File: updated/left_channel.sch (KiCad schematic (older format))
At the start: 20 parts, among them J2 Left 8 ohms, J3 Left 0 ohms, J7 Conn_Coaxial, T1 AudioTxfmr

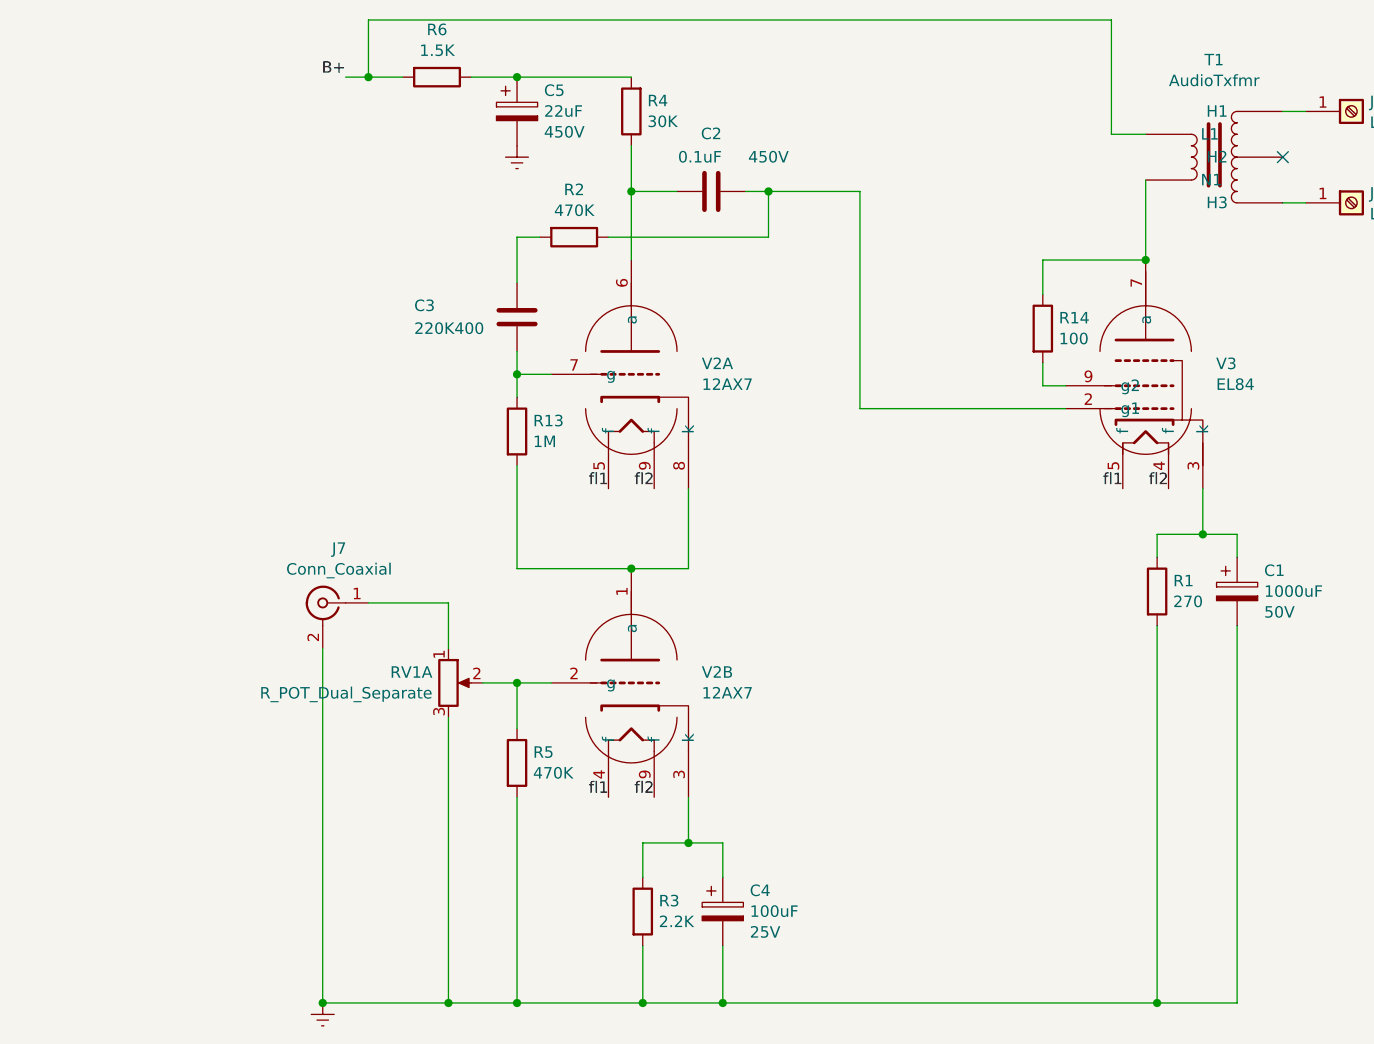
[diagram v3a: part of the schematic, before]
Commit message: adding some components to try to stop a high pitch squal sound I sometimes hear from the amp
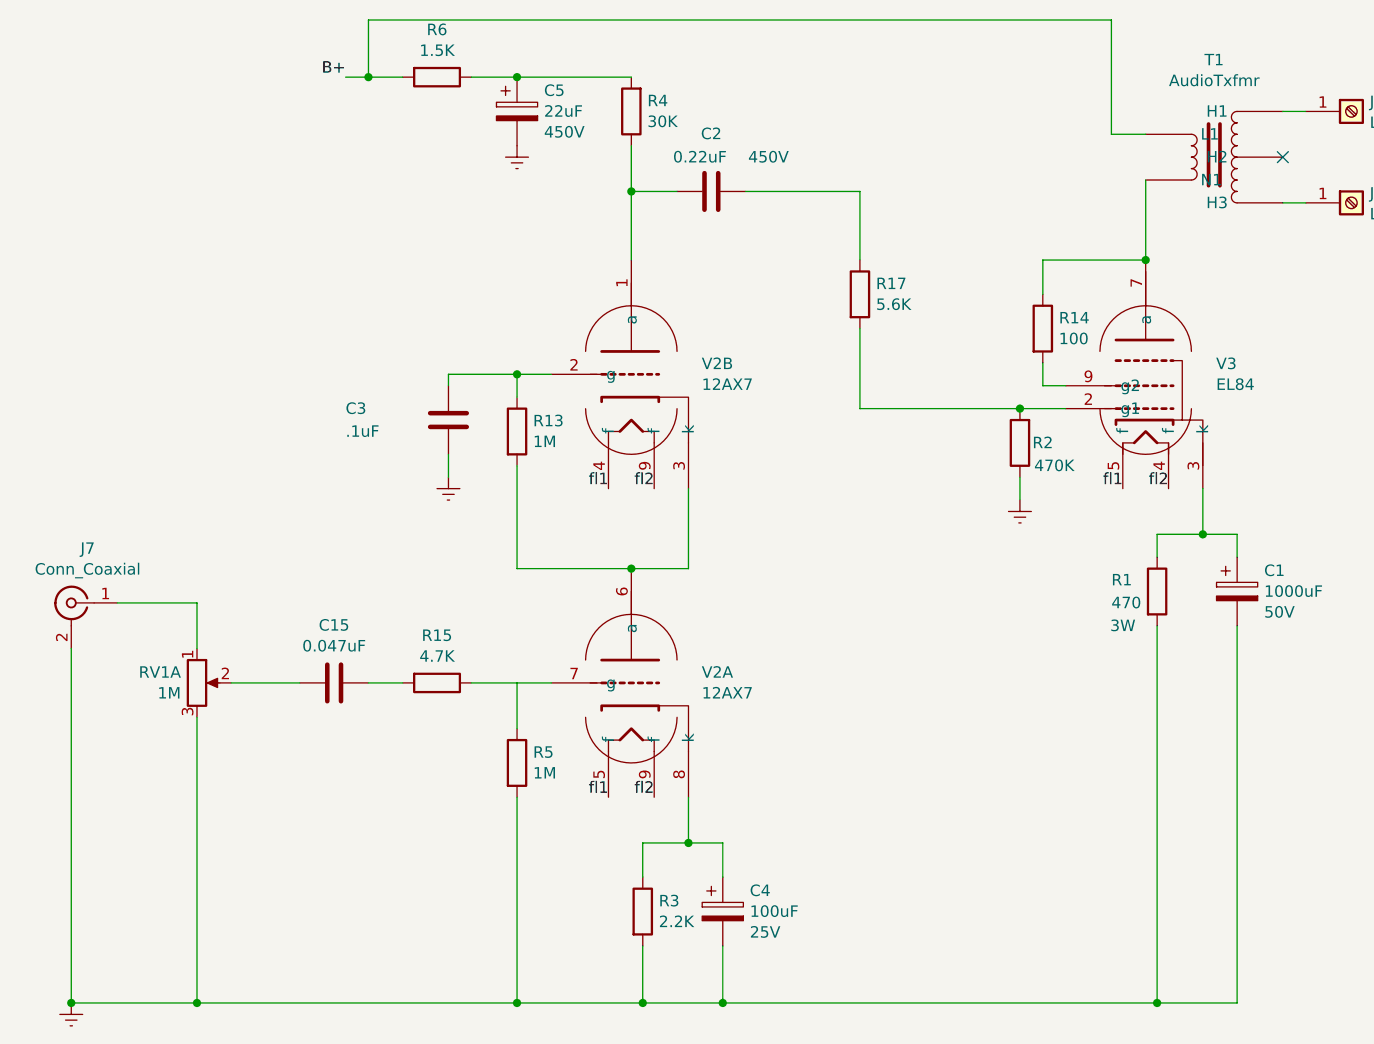
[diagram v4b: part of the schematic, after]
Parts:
- added C15: 0.047uF, symbol Device:C
- added R15: 4.7K, symbol Device:R
- added R17: 5.6K, symbol Device:R
- C2: value 0.1uF -> 0.22uF
- C3: value 220K400 -> .1uF
- R1: value 270 -> 470; Power 5W -> 3W
- R5: value 470K -> 1M
- RV1: value R_POT_Dual_Separate -> 1M
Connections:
- net Earth: now also C3.2, R2.1
- net at C2.2, R4.1: now also V2.1 (a); no longer V2.6 (a)
- net at C4.1, R3.1: now also V2.8 (k); no longer V2.3 (k)
- net at R2.2: now also V3.2 (g1), R17.2; no longer C3.1
- new net: R13.2, V2.3 (k), V2.6 (a)
- new net: R15.1, R5.1, V2.7 (g)
- new net: C3.1, R13.1, V2.2 (g)
- new net: C2.1, R17.1
- new net: C15.2, RV1.2
- new net: C15.1, R15.2
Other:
- moved on the sheet: C3, J7, R2, RV1A, V2A, V2B
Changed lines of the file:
@@
 $Descr A4 11693 8268
 encoding utf-8
-Sheet 3 5
+Sheet 3 4
 Title ""
 Date ""
@@
 AR Path="/5F1F04D2/5F1FED5C" Ref="C2"  Part="1"
 F 0 "C2" V 4898 2350 50  0000 C CNN
-F 1 "0.1uF" V 5000 2300 50  0000 C CNN
+F 1 "0.22uF" V 5000 2300 50  0000 C CNN
 F 2 "Capacitor_THT:CP_Radial_D4.0mm_P2.00mm" H 5188 2200 50  0001 C CNN
 F 3 "~" H 5150 2350 50  0001 C CNN
@@
 L Device:R R?
 U 1 1 5F1FED63
-P 4550 2550
+P 6500 3450
 AR Path="/5F1FED63" Ref="R?"  Part="1"
 AR Path="/5F1F04D2/5F1FED63" Ref="R2"  Part="1"
-F 0 "R2" V 4343 2550 50  0000 C CNN
-F 1 "470K" V 4434 2550 50  0000 C CNN
-F 2 "Resistor_THT:R_Axial_DIN0516_L15.5mm_D5.0mm_P20.32mm_Horizontal" V 4480 2550 50  0001 C CNN
-F 3 "~" H 4550 2550 50  0001 C CNN
-	1    4550 2550
-	0    1    1    0
+F 0 "R2" H 6400 3450 50  0000 C CNN
+F 1 "470K" H 6350 3550 50  0000 C CNN
+F 2 "Resistor_THT:R_Axial_DIN0516_L15.5mm_D5.0mm_P20.32mm_Horizontal" V 6430 3450 50  0001 C CNN
+F 3 "~" H 6500 3450 50  0001 C CNN
+	1    6500 3450
+	-1   0    0    1
 $EndComp
 $Comp
 L Device:C C?
 U 1 1 5F1FED69
-P 4300 2900
+P 4000 3350
 AR Path="/5F1FED69" Ref="C?"  Part="1"
 AR Path="/5F1F04D2/5F1FED69" Ref="C3"  Part="1"
-F 0 "C3" H 3850 2950 50  0000 L CNN
-F 1 "220K400" H 3850 2850 50  0000 L CNN
-F 2 "Capacitor_THT:CP_Radial_D10.0mm_P2.50mm" H 4338 2750 50  0001 C CNN
-F 3 "~" H 4300 2900 50  0001 C CNN
-	1    4300 2900
+F 0 "C3" H 3550 3400 50  0000 L CNN
+F 1 ".1uF" H 3550 3300 50  0000 L CNN
+F 2 "Capacitor_THT:CP_Radial_D10.0mm_P2.50mm" H 4038 3200 50  0001 C CNN
+F 3 "~" H 4000 3350 50  0001 C CNN
+	1    4000 3350
 	1    0    0    -1
 $EndComp
@@
 L Connector:Conn_Coaxial J?
 U 1 1 5F1FED7F
-P 3450 4150
+P 2350 4150
 AR Path="/5F1FED7F" Ref="J?"  Part="1"
 AR Path="/5F1F04D2/5F1FED7F" Ref="J7"  Part="1"
-F 0 "J7" H 3378 4388 50  0000 C CNN
-F 1 "Conn_Coaxial" H 3378 4297 50  0000 C CNN
-F 2 "" H 3450 4150 50  0001 C CNN
-F 3 " ~" H 3450 4150 50  0001 C CNN
-	1    3450 4150
+F 0 "J7" H 2278 4388 50  0000 C CNN
+F 1 "Conn_Coaxial" H 2278 4297 50  0000 C CNN
+F 2 "" H 2350 4150 50  0001 C CNN
+F 3 " ~" H 2350 4150 50  0001 C CNN
+	1    2350 4150
 	-1   0    0    -1
 $EndComp
 Wire Wire Line
-	4000 4650 4000 5900
-Wire Wire Line
-	4000 5900 3450 5900
-Wire Wire Line
-	3450 5900 3450 4350
+	2900 4650 2900 5900
+Wire Wire Line
+	2900 5900 2350 5900
+Wire Wire Line
+	2350 5900 2350 4350
 $Comp
 L power:Earth #PWR?
 U 1 1 5F1FED8E
-P 3450 5900
+P 2350 5900
 AR Path="/5F1FED8E" Ref="#PWR?"  Part="1"
 AR Path="/5F1F04D2/5F1FED8E" Ref="#PWR06"  Part="1"
-F 0 "#PWR06" H 3450 5650 50  0001 C CNN
-F 1 "Earth" H 3450 5750 50  0001 C CNN
-F 2 "" H 3450 5900 50  0001 C CNN
-F 3 "~" H 3450 5900 50  0001 C CNN
-	1    3450 5900
-	1    0    0    -1
-$EndComp
-Connection ~ 3450 5900
-Wire Wire Line
-	3650 4150 4000 4150
-Wire Wire Line
-	4000 4150 4000 4350
-Wire Wire Line
-	4150 4500 4300 4500
+F 0 "#PWR06" H 2350 5650 50  0001 C CNN
+F 1 "Earth" H 2350 5750 50  0001 C CNN
+F 2 "" H 2350 5900 50  0001 C CNN
+F 3 "~" H 2350 5900 50  0001 C CNN
+	1    2350 5900
+	1    0    0    -1
+$EndComp
+Connection ~ 2350 5900
+Wire Wire Line
+	2550 4150 2900 4150
+Wire Wire Line
+	2900 4150 2900 4350
 Text Label 4700 3650 2    50   ~ 0
 fl1
@@
 AR Path="/5F1F04D2/5F1FED9C" Ref="R5"  Part="1"
 F 0 "R5" H 4370 4896 50  0000 L CNN
-F 1 "470K" H 4370 4805 50  0000 L CNN
+F 1 "1M" H 4370 4805 50  0000 L CNN
 F 2 "Resistor_THT:R_Axial_DIN0516_L15.5mm_D5.0mm_P20.32mm_Horizontal" V 4230 4850 50  0001 C CNN
 F 3 "~" H 4300 4850 50  0001 C CNN
@@
 Wire Wire Line
 	4300 4700 4300 4500
-Connection ~ 4300 4500
 Wire Wire Line
 	4300 4500 4450 4500
@@
 $EndComp
 Wire Wire Line
-	4300 5900 4000 5900
+	4300 5900 2900 5900
 Wire Wire Line
 	4300 5000 4300 5900
-Connection ~ 4000 5900
-Connection ~ 4300 5900
+Connection ~ 2900 5900
 Wire Wire Line
 	5200 5650 5200 5900
@@
 	4850 5900 5200 5900
 Wire Wire Line
-	4300 3050 4300 3150
-Wire Wire Line
 	4450 3150 4300 3150
-Connection ~ 4300 3150
 Wire Wire Line
 	4300 3150 4300 3250
-Wire Wire Line
-	5300 2350 5400 2350
-Wire Wire Line
-	4400 2550 4300 2550
-Wire Wire Line
-	4300 2550 4300 2750
-Wire Wire Line
-	4700 2550 5400 2550
-Wire Wire Line
-	5400 2550 5400 2350
-Connection ~ 5400 2350
-Wire Wire Line
-	5400 2350 5800 2350
 NoConn ~ 7650 2200
 $Comp
@@
 	7750 2000 7650 2000
 Wire Wire Line
-	6700 3300 5800 3300
-Wire Wire Line
-	5800 3300 5800 2350
+	6700 3300 6500 3300
 Text Label 6950 3650 2    50   ~ 0
 fl1
@@
 AR Path="/5F1FEE00" Ref="R?"  Part="1"
 AR Path="/5F1F04D2/5F1FEE00" Ref="R1"  Part="1"
-F 0 "R1" H 7170 4146 50  0000 L CNN
-F 1 "270" H 7170 4055 50  0000 L CNN
+F 0 "R1" H 6900 4150 50  0000 L CNN
+F 1 "470" H 6900 4050 50  0000 L CNN
 F 2 "Resistor_THT:R_Axial_DIN0516_L15.5mm_D5.0mm_P20.32mm_Horizontal" V 7030 4100 50  0001 C CNN
 F 3 "~" H 7100 4100 50  0001 C CNN
-F 4 "5W" H 7100 4100 50  0001 C CNN "Power"
+F 4 "3W" H 6950 3950 50  0000 C CNN "Power"
 	1    7100 4100
 	1    0    0    -1
@@
 L local:12AX7 V2
 U 1 1 5F1EB7D2
+P 4800 4450
+F 0 "V2" H 5108 4446 50  0000 L CNN
+F 1 "12AX7" H 5108 4355 50  0000 L CNN
+F 2 "Valve:Valve_ECC-83-1" H 4820 4450 50  0001 C CNN
+F 3 "" H 4820 4450 50  0001 C CNN
+	1    4800 4450
+	1    0    0    -1
+$EndComp
+Wire Wire Line
+	4300 4000 4800 4000
+$Comp
+L local:12AX7 V2
+U 2 1 5F1F6427
 P 4800 3100
 F 0 "V2" H 5108 3096 50  0000 L CNN
@@
 F 2 "Valve:Valve_ECC-83-1" H 4820 3100 50  0001 C CNN
 F 3 "" H 4820 3100 50  0001 C CNN
-	1    4800 3100
-	1    0    0    -1
-$EndComp
-Wire Wire Line
-	4300 4000 4800 4000
-$Comp
-L local:12AX7 V2
-U 2 1 5F1F6427
-P 4800 4450
-F 0 "V2" H 5108 4446 50  0000 L CNN
-F 1 "12AX7" H 5108 4355 50  0000 L CNN
-F 2 "Valve:Valve_ECC-83-1" H 4820 4450 50  0001 C CNN
-F 3 "" H 4820 4450 50  0001 C CNN
-	2    4800 4450
+	2    4800 3100
 	1    0    0    -1
 $EndComp
@@
 L Device:R_POT_Dual_Separate RV1
 U 1 1 5F23DDB3
-P 4000 4500
-F 0 "RV1" H 3930 4546 50  0000 R CNN
-F 1 "R_POT_Dual_Separate" H 3930 4455 50  0000 R CNN
-F 2 "" H 4000 4500 50  0001 C CNN
-F 3 "~" H 4000 4500 50  0001 C CNN
-	1    4000 4500
-	1    0    0    -1
-$EndComp
+P 2900 4500
+F 0 "RV1" H 2830 4546 50  0000 R CNN
+F 1 "1M" H 2830 4455 50  0000 R CNN
+F 2 "" H 2900 4500 50  0001 C CNN
+F 3 "~" H 2900 4500 50  0001 C CNN
+	1    2900 4500
+	1    0    0    -1
+$EndComp
+$Comp
+L Device:C C?
+U 1 1 5F5B00D6
+P 3500 4500
+AR Path="/5F200EB9/5F5B00D6" Ref="C?"  Part="1"
+AR Path="/5F1F04D2/5F5B00D6" Ref="C15"  Part="1"
+F 0 "C15" V 3248 4500 50  0000 C CNN
+F 1 "0.047uF" V 3339 4500 50  0000 C CNN
+F 2 "" H 3538 4350 50  0001 C CNN
+F 3 "~" H 3500 4500 50  0001 C CNN
+	1    3500 4500
+	0    1    1    0
+$EndComp
+$Comp
+L Device:R R?
+U 1 1 5F5B00DC
+P 3950 4500
+AR Path="/5F200EB9/5F5B00DC" Ref="R?"  Part="1"
+AR Path="/5F1F04D2/5F5B00DC" Ref="R15"  Part="1"
+F 0 "R15" V 3743 4500 50  0000 C CNN
+F 1 "4.7K" V 3834 4500 50  0000 C CNN
+F 2 "" V 3880 4500 50  0001 C CNN
+F 3 "~" H 3950 4500 50  0001 C CNN
+	1    3950 4500
+	0    1    1    0
+$EndComp
+Wire Wire Line
+	3650 4500 3800 4500
+Wire Wire Line
+	4100 4500 4300 4500
+Wire Wire Line
+	3050 4500 3350 4500
+Connection ~ 4300 5900
+$Comp
+L power:Earth #PWR?
+U 1 1 5F5C6D43
+P 6500 3700
+AR Path="/5F200EB9/5F5C6D43" Ref="#PWR?"  Part="1"
+AR Path="/5F1F04D2/5F5C6D43" Ref="#PWR011"  Part="1"
+F 0 "#PWR011" H 6500 3450 50  0001 C CNN
+F 1 "Earth" H 6500 3550 50  0001 C CNN
+F 2 "" H 6500 3700 50  0001 C CNN
+F 3 "~" H 6500 3700 50  0001 C CNN
+	1    6500 3700
+	1    0    0    -1
+$EndComp
+Wire Wire Line
+	6500 3700 6500 3600
+Connection ~ 6500 3300
+Wire Wire Line
+	6500 3300 5800 3300
+Wire Wire Line
+	5300 2350 5800 2350
+$Comp
+L power:Earth #PWR?
+U 1 1 5F5E593F
+P 4000 3600
+AR Path="/5F200EB9/5F5E593F" Ref="#PWR?"  Part="1"
+AR Path="/5F1F04D2/5F5E593F" Ref="#PWR010"  Part="1"
+F 0 "#PWR010" H 4000 3350 50  0001 C CNN
+F 1 "Earth" H 4000 3450 50  0001 C CNN
+F 2 "" H 4000 3600 50  0001 C CNN
+F 3 "~" H 4000 3600 50  0001 C CNN
+	1    4000 3600
+	1    0    0    -1
+$EndComp
+Wire Wire Line
+	4000 3600 4000 3500
+Wire Wire Line
+	4300 3150 4000 3150
+Wire Wire Line
+	4000 3150 4000 3200
+Connection ~ 4300 3150
+$Comp
+L Device:R R?
+U 1 1 5F5F04AC
+P 5800 2800
+AR Path="/5F200EB9/5F5F04AC" Ref="R?"  Part="1"
+AR Path="/5F1F04D2/5F5F04AC" Ref="R17"  Part="1"
+F 0 "R17" H 5870 2846 50  0000 L CNN
+F 1 "5.6K" H 5870 2755 50  0000 L CNN
+F 2 "" V 5730 2800 50  0001 C CNN
+F 3 "~" H 5800 2800 50  0001 C CNN
+	1    5800 2800
+	1    0    0    -1
+$EndComp
+Wire Wire Line
+	5800 2650 5800 2350
+Wire Wire Line
+	5800 2950 5800 3300
 $EndSCHEMATC

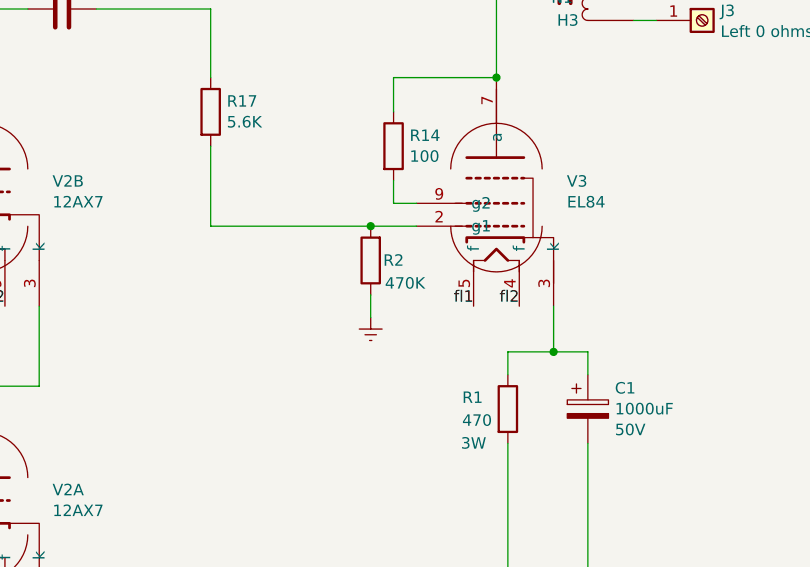
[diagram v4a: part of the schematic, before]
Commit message: change EL84 grid leak resistor to 1M
In the day time, I sort of feel the amp is too quiet. That adding the 5.6k resistor inline has reduced the signal. This small resistance divide is like 98% the input. But that is still the 2% loss of signal. I think the gain stage of these preamp tubes is not very strong. And I read the EL84 does have a wider response to small changes in input impedance.
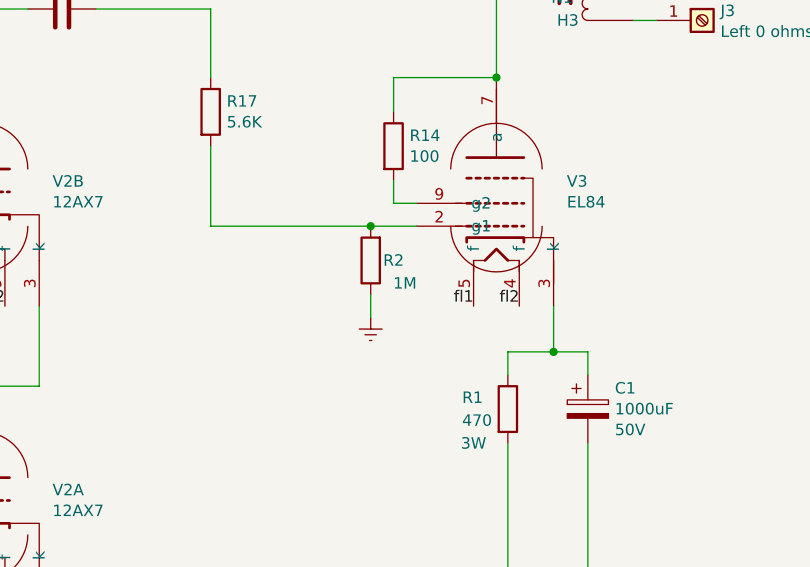
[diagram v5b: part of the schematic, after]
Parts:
- R2: value 470K -> 1M
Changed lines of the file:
@@
 AR Path="/5F1F04D2/5F1FED63" Ref="R2"  Part="1"
 F 0 "R2" H 6400 3450 50  0000 C CNN
-F 1 "470K" H 6350 3550 50  0000 C CNN
+F 1 "1M" H 6350 3550 50  0000 C CNN
 F 2 "Resistor_THT:R_Axial_DIN0516_L15.5mm_D5.0mm_P20.32mm_Horizontal" V 6430 3450 50  0001 C CNN
 F 3 "~" H 6500 3450 50  0001 C CNN

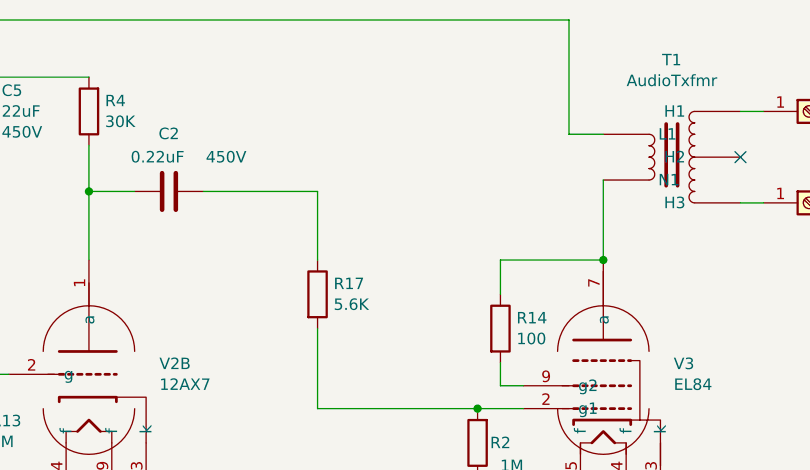
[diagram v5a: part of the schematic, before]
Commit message: install vfd spectrograph
upgrade preamp tubes to use shielded sockets.
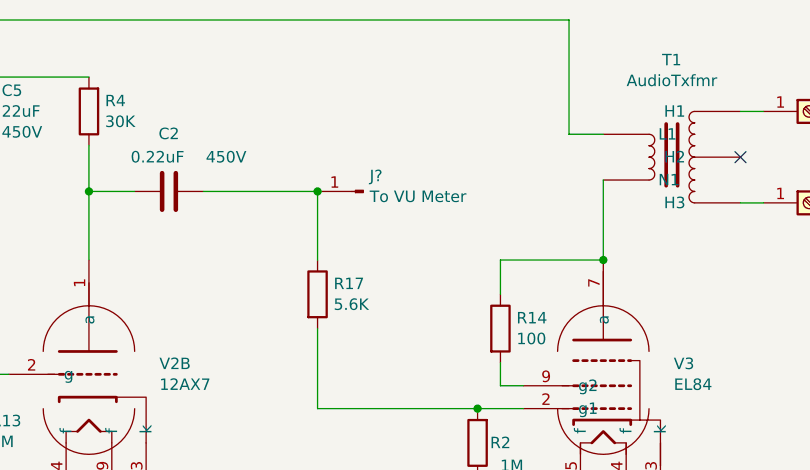
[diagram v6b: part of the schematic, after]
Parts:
- added J?: To VU Meter, symbol Connector:Conn_01x01_Male
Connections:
- net at C2.1, R17.1: now also J?.1 (Pin_1)
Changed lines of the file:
@@
 Wire Wire Line
 	5800 2950 5800 3300
+$Comp
+L Connector:Conn_01x01_Male J?
+U 1 1 5F53BD18
+P 6000 2350
+F 0 "J?" H 5972 2282 50  0000 R CNN
+F 1 "To VU Meter" H 5972 2373 50  0000 R CNN
+F 2 "" H 6000 2350 50  0001 C CNN
+F 3 "~" H 6000 2350 50  0001 C CNN
+	1    6000 2350
+	-1   0    0    1
+$EndComp
+Connection ~ 5800 2350
 $EndSCHEMATC
